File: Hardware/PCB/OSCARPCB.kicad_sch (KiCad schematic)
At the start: 0 parts

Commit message: Added ESP32 Cam
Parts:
- added A1: ESP32_CAM, PCM_SL_Development_Boards:ESP32-CAM, symbol PCM_SL_Development_Board:ESP32_CAM
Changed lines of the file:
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@@
 	(generator_version "9.0")
 	(paper "A4")
+	(symbol
+		(lib_id "PCM_SL_Development_Board:ESP32_CAM")
+		(at 115.57 82.55 0)
+		(unit 1)
+		(exclude_from_sim no)
+		(in_bom yes)
+		(on_board yes)
+		(dnp no)
+		(fields_autoplaced yes)
+		(property "Reference" "A1"
+			(at 115.57 62.23 0)
+			(effects
+				(font
+					(size 1.27 1.27)
+				)
+			)
+		)
+		(property "Value" "ESP32_CAM"
+			(at 115.57 64.77 0)
+			(effects
+				(font
+					(size 1.27 1.27)
+				)
+			)
+		)
+		(property "Footprint" "PCM_SL_Development_Boards:ESP32-CAM"
+			(at 114.3 90.17 0)
+			(effects
+				(font
+					(size 1.27 1.27)
+				)
+				(hide yes)
+			)
+		)
+		(property "Datasheet" ""
+			(at 99.06 68.58 0)
+			(effects
+				(font
+					(size 1.27 1.27)
+				)
+				(hide yes)
+			)
+		)
+		(property "Description" "ESP32-S SoC with onboard camera and MicroSD card support."
+			(at 115.57 82.55 0)
+			(effects
+				(font
+					(size 1.27 1.27)
+				)
+				(hide yes)
+			)
+		)
+		(pin "13"
+		)
+		(pin "12"
+		)
+		(pin "6"
+		)
+		(pin "15"
+		)
+		(pin "14"
+		)
+		(pin "9"
+		)
+		(pin "3"
+		)
+		(pin "7"
+		)
+		(pin "11"
+		)
+		(pin "2"
+		)
+		(pin "5"
+		)
+		(pin "8"
+		)
+		(pin "16"
+		)
+		(pin "10"
+		)
+		(pin "1"
+		)
+		(pin "4"
+		)
+		(instances
+			(project ""
+				(path "/64e74c02-7eb2-4c7e-9a31-0fe61f345101"
+					(reference "A1")
+					(unit 1)
+				)
+			)
+		)
+	)
 	(sheet_instances
 		(path "/"

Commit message: Started PCB schematic
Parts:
- added A2: Pololu_Breakout_DRV8825, Module:Pololu_Breakout-16_15.2x20.3mm, symbol Driver_Motor:Pololu_Breakout_DRV8825
- added C1: 220uF_50V, Capacitor_THT:CP_Radial_D10.0mm_P5.00mm, symbol PCM_SL_Capacitors:220uF_50V
- added J1: CP2102 IN, Connector_PinSocket_2.54mm:PinSocket_1x06_P2.54mm_Vertical, symbol PCM_SL_Pin_Headers:PINHD_1x6_Female
- added J2: Stepper Motor OUT, Connector_JST:JST_EH_B4B-EH-A_1x04_P2.50mm_Vertical, symbol PCM_SL_Connectors:JST_04
- added J3: DC Motors OUT, Connector_PinSocket_2.54mm:PinSocket_1x04_P2.54mm_Vertical, symbol PCM_SL_Pin_Headers:PINHD_1x4_Female
- added J4: Battery, Connector_JST:JST_EH_B2B-EH-A_1x02_P2.50mm_Vertical, symbol PCM_SL_Connectors:JST_02
- added U1: L293D, Package_DIP:DIP-16_W7.62mm, symbol Driver_Motor:L293D
- added U2: ESP32-DevKitC, PCM_Espressif:ESP32-DevKitC, symbol PCM_Espressif:ESP32-DevKitC
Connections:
- net GND: now reaches A1.13 (GND)
- net GND: now also A1.2 (GND), A1.9 (GND), A2.1 (GND), A2.7 (GND), C1.2, U1.12 (GND), U1.13 (GND), U1.4 (GND), U1.5 (GND), U2.14 (GND), U2.32 (GND), U2.38 (GND)
- new net L Motor +: J3.1, U1.3 (1Y)
- new net L Motor -: J3.2, U1.6 (2Y)
- new net L Motor 1: U1.2 (1A), U2.11 (ADC2_CH7/GPIO27)
- new net L Motor 2: U1.7 (2A), U2.20 (SD_CLK/GPIO6)
- new net L Motor EN: U1.1 (EN1,2), U2.21 (SD_DATA0/GPIO7)
- new net NC: U2.16 (SD_DATA2/GPIO9), U2.17 (SD_DATA3/GPIO10), U2.18 (CMD)
- new net R Motor +: J3.3, U1.11 (3Y)
- new net R Motor -: J3.4, U1.14 (4Y)
- new net R Motor 3: U1.10 (3A), U2.22 (SD_DATA1/GPIO8)
- new net R Motor 4: U1.15 (4A), U2.27 (GPIO16)
- new net R Motor EN: U1.9 (EN3,4), U2.28 (GPIO17)
- new net S. A1: A2.4 (A1), J2.1
- new net S. A2: A2.3 (A2), J2.2
- new net S. B1: A2.5 (B1), J2.3
- new net S. B2: A2.6 (B2), J2.4
- new net S. DIR: A2.16 (DIR), U2.36 (GPIO22)
- new net S. EN: A2.9 (~{EN}), U2.31 (GPIO19)
- new net S. FLT: A2.2 (~{FLT}), U2.29 (GPIO5)
- new net S. M0: A2.10 (M0), U2.37 (GPIO23)
- new net S. M1: A2.11 (M1), U2.9 (DAC_1/ADC2_CH8/GPIO25)
- new net S. M2: A2.12 (M2), U2.10 (DAC_2/ADC2_CH9/GPIO26)
- new net S. SLP + RST: A2.13 (~{RST}), A2.14 (~{SLP}), U2.30 (GPIO18)
- new net S. STEP: A2.15 (STEP), U2.33 (GPIO21)
- new net VMOT: A2.8 (VMOT), C1.1
- new net Vdrive: U1.16 (VCC1), U1.8 (VCC2)
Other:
- note added: "Camera"
- moved on the sheet: A1

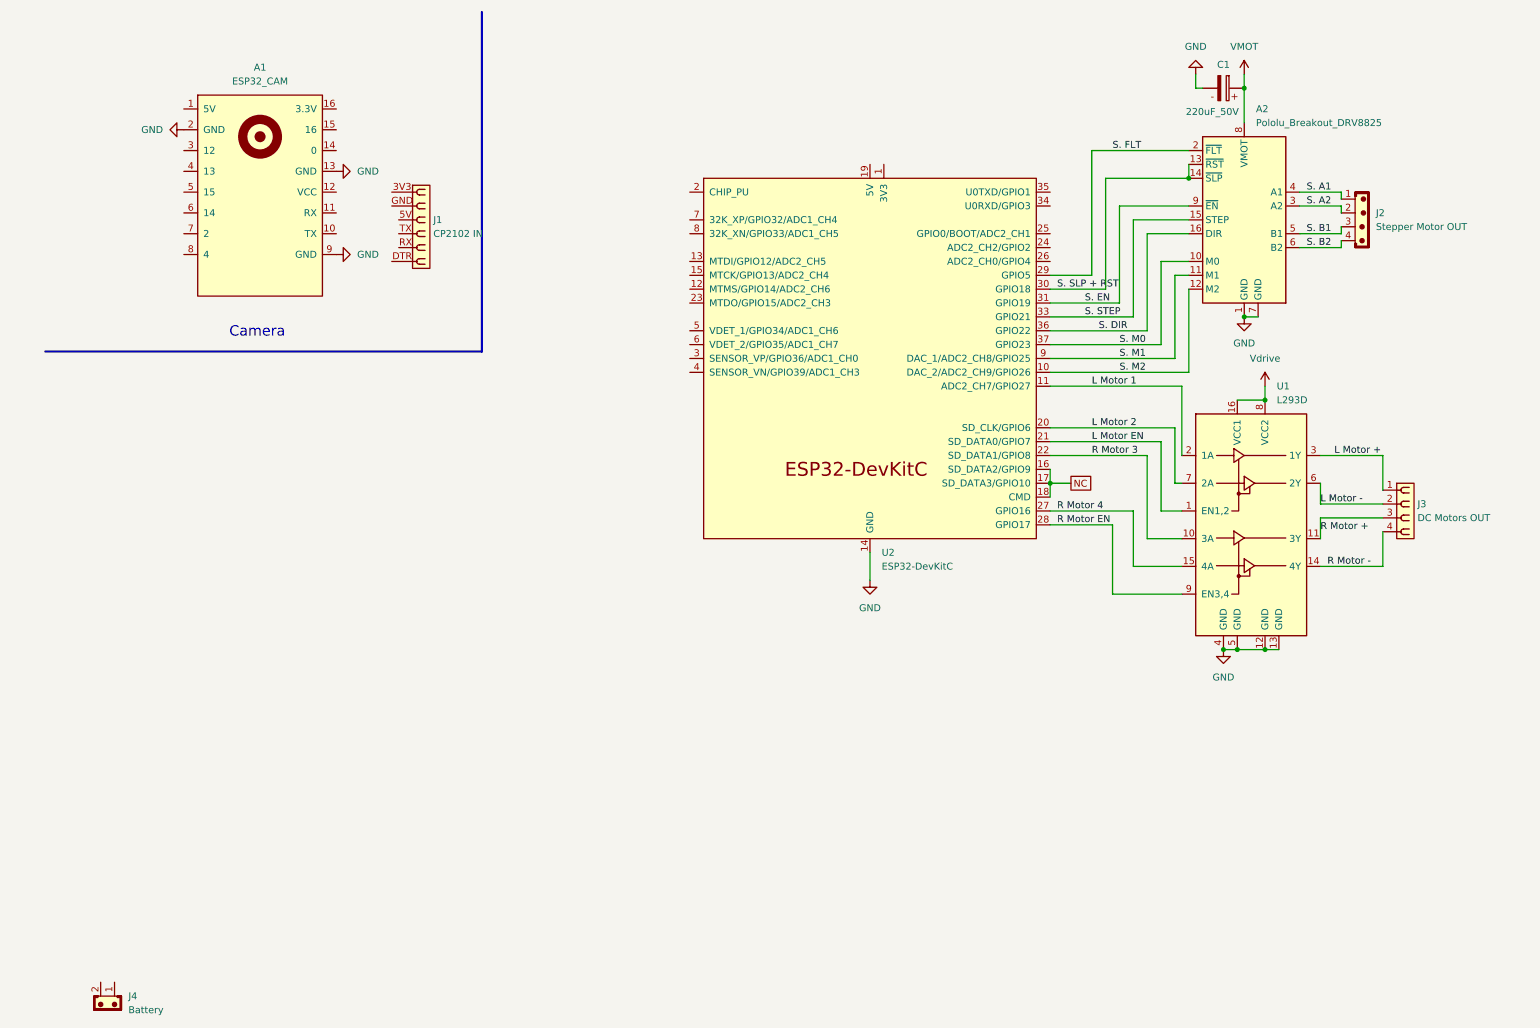
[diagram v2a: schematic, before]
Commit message: Started routing PCB
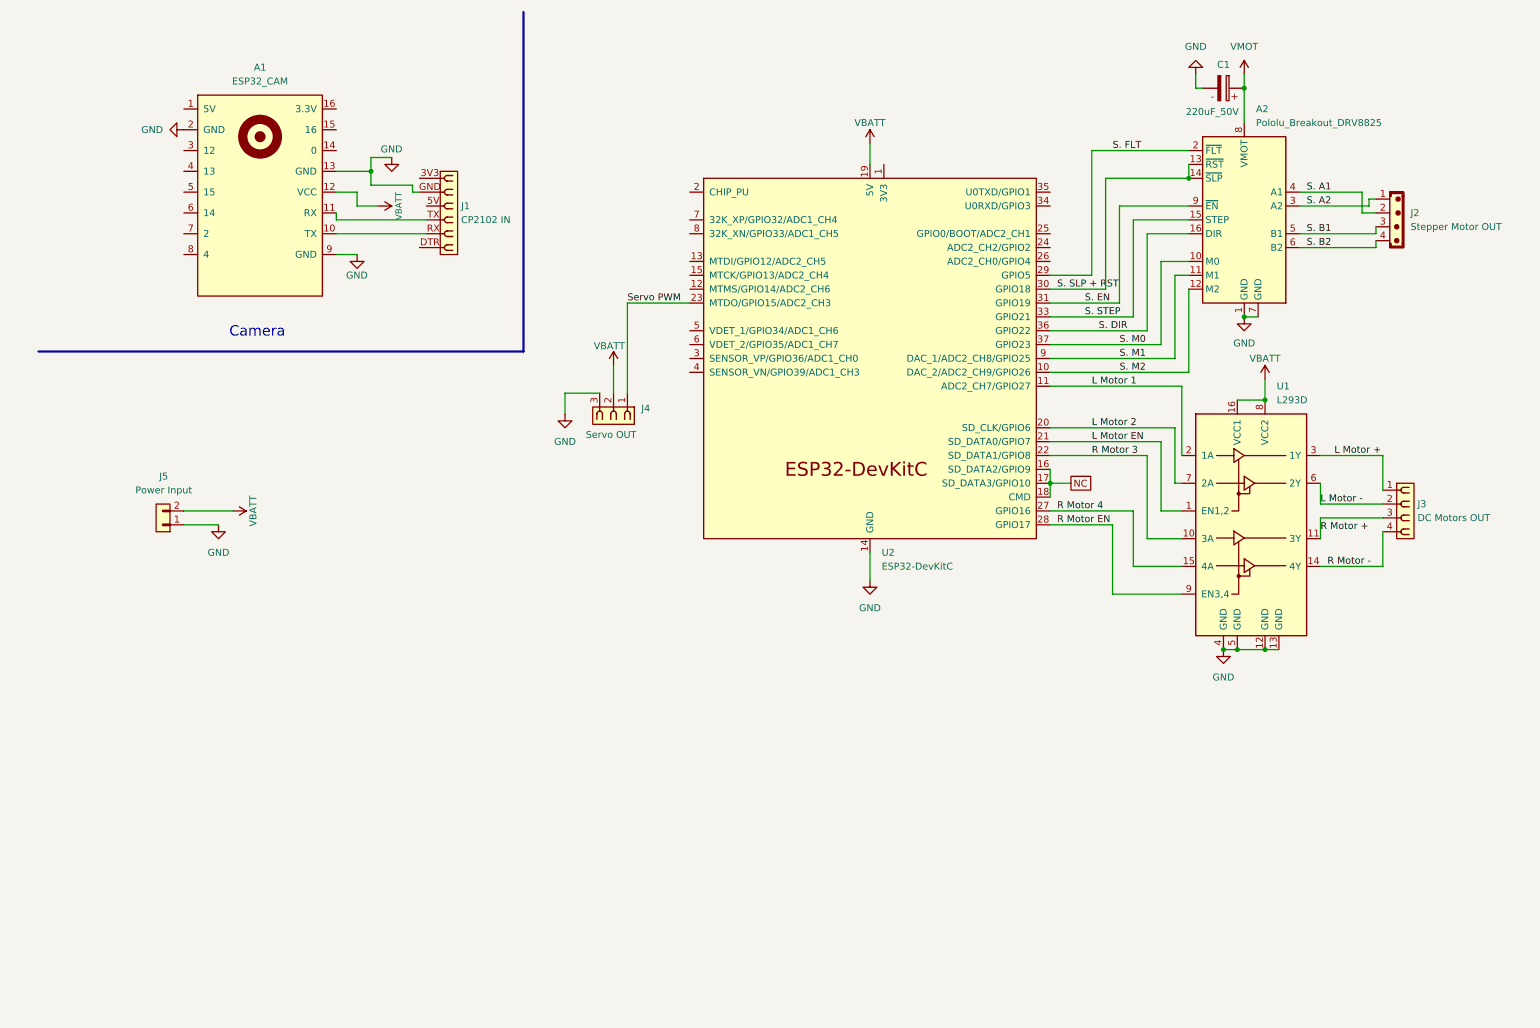
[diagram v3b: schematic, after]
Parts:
- removed J4: Battery, Connector_JST:JST_EH_B2B-EH-A_1x02_P2.50mm_Vertical, symbol PCM_SL_Connectors:JST_02
- added J4: Servo OUT, Connector_PinSocket_2.54mm:PinSocket_1x03_P2.54mm_Vertical, symbol PCM_SL_Pin_Headers:PINHD_1x3_Female
- added J5: Power Input, Connector_PinHeader_2.54mm:PinHeader_1x02_P2.54mm_Vertical, symbol PCM_SL_Pin_Headers:PINHD_1x2_Male
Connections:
- net Vdrive is gone; now on net VBATT: U1.16 (VCC1), U1.8 (VCC2)
- net GND: now also J1.GND, J4.3, J5.1
- net S. A1: now also J2.2; no longer J2.1
- net S. A2: now also J2.1; no longer J2.2
- net at A1.10 (TX): now also J1.RX
- net at A1.11 (RX): now also J1.TX
- net VBATT: now reaches A1.12 (VCC)
- net VBATT: now also U2.19 (5V), J4.2, J5.2
- net Servo PWM: now reaches U2.23 (MTDO/GPIO15/ADC2_CH3)
- net Servo PWM: now also J4.1
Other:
- moved on the sheet: J1, J2

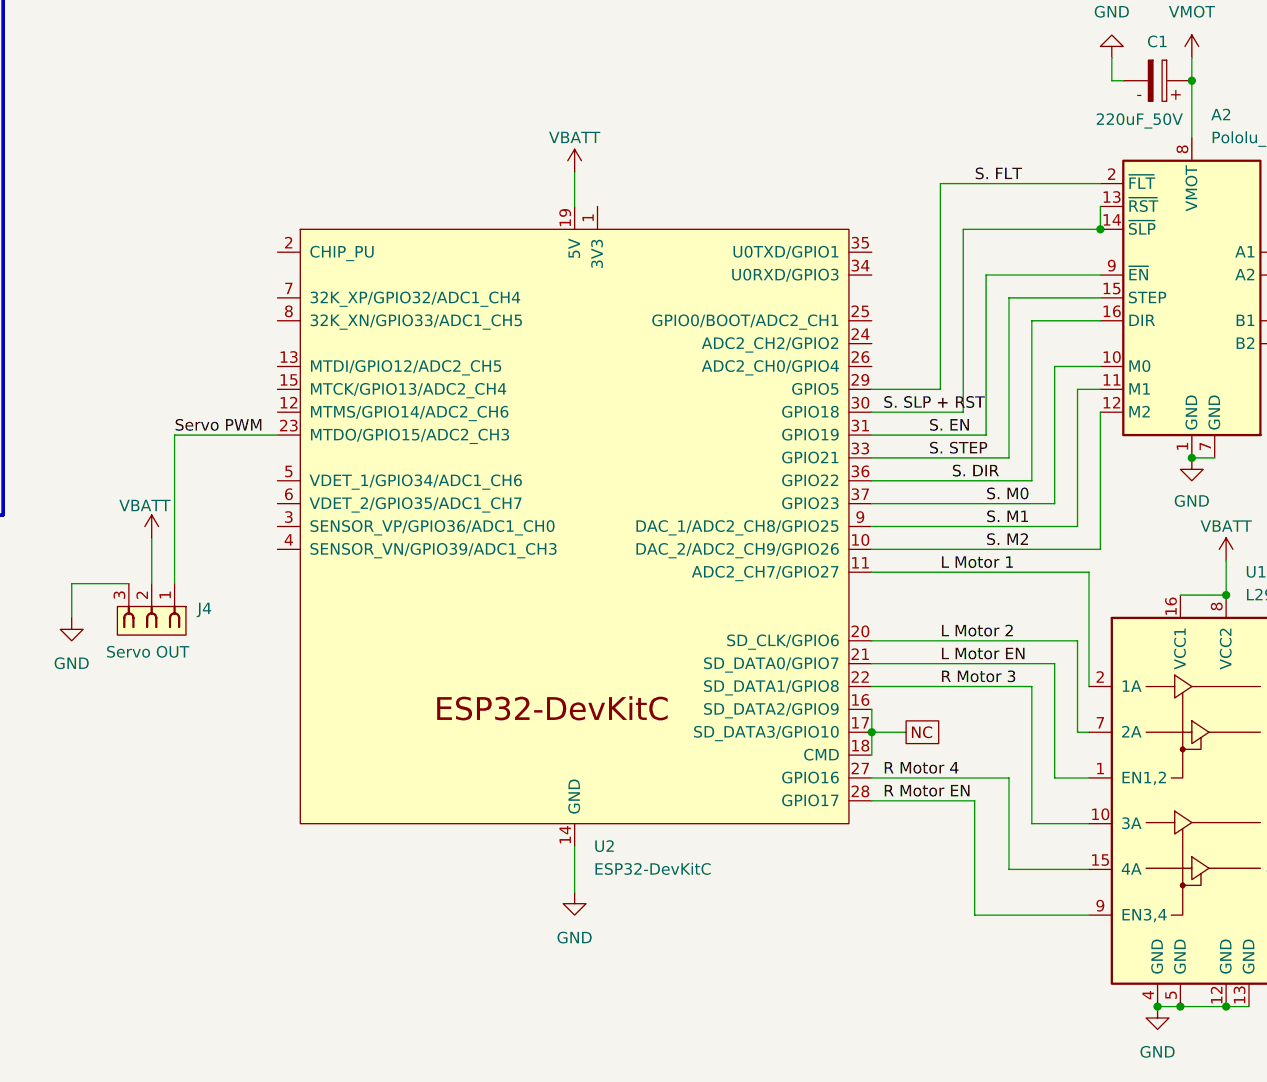
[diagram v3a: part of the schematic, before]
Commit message: changed sch to fit PCB better
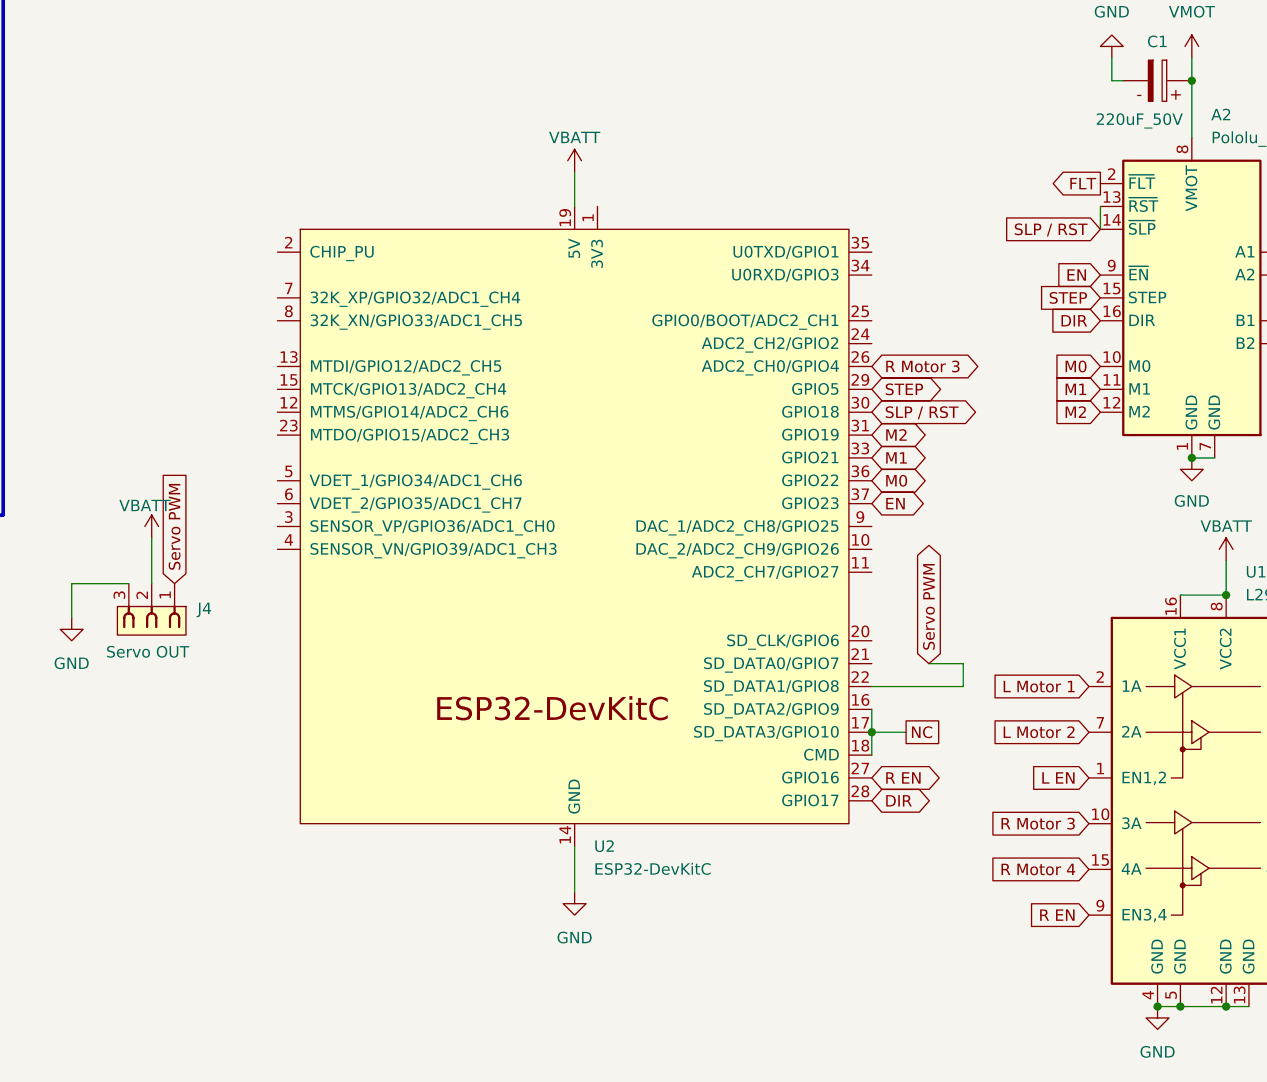
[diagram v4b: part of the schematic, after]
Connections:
- net L Motor 1: no longer U2.11 (ADC2_CH7/GPIO27)
- net L Motor 2: no longer U2.20 (SD_CLK/GPIO6)
- net R Motor 3: now also U2.26 (ADC2_CH0/GPIO4); no longer U2.22 (SD_DATA1/GPIO8)
- net R Motor 4: no longer U2.27 (GPIO16)
- net Servo PWM: now also U2.22 (SD_DATA1/GPIO8); no longer U2.23 (MTDO/GPIO15/ADC2_CH3)
- net L Motor EN: no longer names the net of U2.21 (SD_DATA0/GPIO7)
- net L Motor EN: no longer U1.1 (EN1,2)
- net R Motor EN renamed DIR
- net DIR: now also A2.16 (DIR); no longer U1.9 (EN3,4)
- net S. DIR renamed M0
- net M0: now also A2.10 (M0); no longer A2.16 (DIR)
- net S. EN renamed EN
- net EN: now also U2.37 (GPIO23); no longer U2.31 (GPIO19)
- net S. FLT renamed FLT
- net FLT: no longer U2.29 (GPIO5)
- removed net S. M0: A2.10 (M0), U2.37 (GPIO23)
- net S. M1: no longer names the net of U2.9 (DAC_1/ADC2_CH8/GPIO25)
- net S. M1: no longer A2.11 (M1)
- net S. M2: no longer names the net of U2.10 (DAC_2/ADC2_CH9/GPIO26)
- net S. M2: no longer A2.12 (M2)
- net S. SLP + RST renamed SLP / RST
- net S. STEP renamed M1
- net M1: now also A2.11 (M1); no longer A2.15 (STEP)
- new net L EN: U1.1 (EN1,2)
- new net M2: A2.12 (M2), U2.31 (GPIO19)
- new net R EN: U1.9 (EN3,4), U2.27 (GPIO16)
- new net STEP: A2.15 (STEP), U2.29 (GPIO5)

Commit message: PCB V1
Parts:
- removed A1: ESP32_CAM, PCM_SL_Development_Boards:ESP32-CAM, symbol PCM_SL_Development_Board:ESP32_CAM
- removed J1: CP2102 IN, Connector_PinSocket_2.54mm:PinSocket_1x06_P2.54mm_Vertical, symbol PCM_SL_Pin_Headers:PINHD_1x6_Female
- added J6: PINHD_1x2_Female, Connector_PinSocket_2.54mm:PinSocket_1x02_P2.54mm_Vertical, symbol PCM_SL_Pin_Headers:PINHD_1x2_Female
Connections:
- net L Motor 1 is gone; now on an unnamed net: U1.2 (1A)
- net L Motor 2 is gone; now on an unnamed net: U1.7 (2A)
- net GND: now also J6.2; no longer A2.7 (GND), C1.2
- net R Motor 4: now also U2.24 (ADC2_CH2/GPIO2)
- net VBATT: now also J6.1
- net at U2.15 (MTCK/GPIO13/ADC2_CH4): now also J4.1
- net L EN: no longer names the net of U1.1 (EN1,2)
- net L EN: now also U2.22 (SD_DATA1/GPIO8)
- removed net NC: U2.16 (SD_DATA2/GPIO9), U2.17 (SD_DATA3/GPIO10), U2.18 (CMD)
- removed net Servo PWM: J4.1, U2.22 (SD_DATA1/GPIO8)
- new net GND VMOT: A2.7 (GND), C1.2
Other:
- note added: "DONT FORGET TO CONNECT CP2102 TO ESP THIS IS ONLY POWER"
